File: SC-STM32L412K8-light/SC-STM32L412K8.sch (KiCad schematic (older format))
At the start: 66 parts, among them J1 usb, J10 Buzzer, J11 Vibro, J12 +3v, J13 +vibro, J2 +29.6 SiPM, J3 TxD (20), J4 RxD (19), J5 SWDIO, J6 SWCLK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

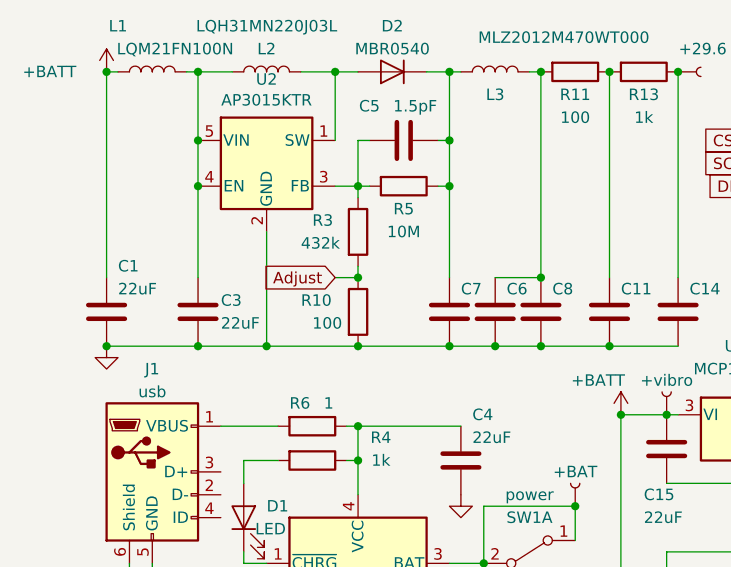
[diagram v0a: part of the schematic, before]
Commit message: изменено:      SC-STM32L412K8-light/SC-STM32L412K8.sch 	изменено:      SC-STM32L412K8-light/SC-STM32L412K8.sch-bak
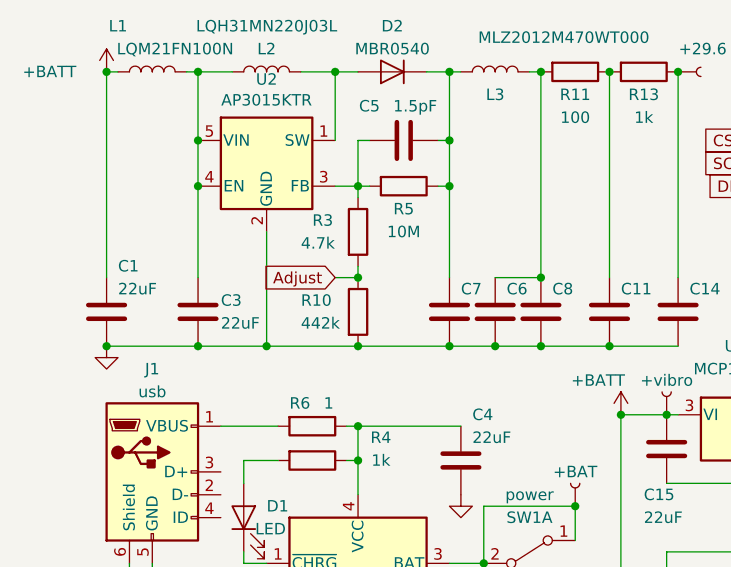
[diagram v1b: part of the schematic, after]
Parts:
- R10: value 100 -> 442k
- R3: value 432k -> 4.7k
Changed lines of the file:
@@
 P 5000 2000
 F 0 "R3" H 4800 2050 50  0000 L CNN
-F 1 "432k" H 4750 1950 50  0000 L CNN
+F 1 "4.7k" H 4750 1950 50  0000 L CNN
 F 2 "Resistor_SMD:R_0603_1608Metric" V 4930 2000 50  0001 C CNN
 F 3 "~" H 5000 2000 50  0001 C CNN
@@
 P 5000 2350
 F 0 "R10" H 4750 2400 50  0000 L CNN
-F 1 "100" H 4800 2300 50  0000 L CNN
+F 1 "442k" H 4750 2300 50  0000 L CNN
 F 2 "Resistor_SMD:R_0603_1608Metric" V 4930 2350 50  0001 C CNN
 F 3 "~" H 5000 2350 50  0001 C CNN
